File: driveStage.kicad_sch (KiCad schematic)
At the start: 20 parts

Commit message: minor improvements
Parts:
- added R?: 0, symbol Device:R
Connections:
- net at R?.2: now also R?.1; no longer R?.2
- new net: R?.2, R?.2
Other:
- note added: "40Hz Sallen-Key low-pass filter Works together with MAX5719 2k output resistance"
- note added: "For control loop response tuning ->"
- note added: "Modulation Depth"
- note removed: "40Hz Sallen-Key low-Pass filter Works together with MAX5719 2k output resistance"
- moved on the sheet: Q?, R?
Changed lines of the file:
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@@
     (stroke (width 0) (type default) (color 0 0 0 0))
   )
-  (wire (pts (xy 278.13 130.81) (xy 278.13 127))
+  (wire (pts (xy 289.56 130.81) (xy 289.56 127))
     (stroke (width 0) (type default) (color 0 0 0 0))
   )
@@
     (stroke (width 0) (type default) (color 0 0 0 0))
   )
-  (wire (pts (xy 271.78 156.21) (xy 274.32 156.21))
-    (stroke (width 0) (type default) (color 0 0 0 0))
-  )
   (wire (pts (xy 236.22 146.05) (xy 241.3 146.05))
     (stroke (width 0) (type default) (color 0 0 0 0))
@@
     (stroke (width 0) (type default) (color 0 0 0 0))
   )
-  (wire (pts (xy 260.35 135.89) (xy 270.51 135.89))
+  (wire (pts (xy 260.35 135.89) (xy 281.94 135.89))
     (stroke (width 0) (type default) (color 0 0 0 0))
   )
@@
     (stroke (width 0) (type default) (color 0 0 0 0))
   )
-  (wire (pts (xy 278.13 127) (xy 285.75 127))
+  (wire (pts (xy 289.56 127) (xy 297.18 127))
     (stroke (width 0) (type default) (color 0 0 0 0))
   )
@@
     (stroke (width 0) (type default) (color 0 0 0 0))
   )
-  (wire (pts (xy 260.35 161.29) (xy 274.32 161.29))
+  (wire (pts (xy 280.67 161.29) (xy 285.75 161.29))
     (stroke (width 0) (type default) (color 0 0 0 0))
   )
@@
     (stroke (width 0) (type default) (color 0 0 0 0))
   )
+  (wire (pts (xy 271.78 156.21) (xy 275.59 156.21))
+    (stroke (width 0) (type default) (color 0 0 0 0))
+  )
   (wire (pts (xy 163.83 163.83) (xy 163.83 166.37))
     (stroke (width 0) (type default) (color 0 0 0 0))
@@
     (stroke (width 0) (type default) (color 0 0 0 0))
   )
+  (wire (pts (xy 283.21 156.21) (xy 285.75 156.21))
+    (stroke (width 0) (type default) (color 0 0 0 0))
+  )
   (wire (pts (xy 171.45 110.49) (xy 185.42 110.49))
     (stroke (width 0) (type default) (color 0 0 0 0))
@@
     (stroke (width 0) (type default) (color 0 0 0 0))
   )
-  (wire (pts (xy 278.13 123.19) (xy 285.75 123.19))
+  (wire (pts (xy 289.56 123.19) (xy 297.18 123.19))
     (stroke (width 0) (type default) (color 0 0 0 0))
   )
@@
     (stroke (width 0) (type default) (color 0 0 0 0))
   )
-  (wire (pts (xy 278.13 118.11) (xy 278.13 123.19))
+  (wire (pts (xy 289.56 118.11) (xy 289.56 123.19))
     (stroke (width 0) (type default) (color 0 0 0 0))
   )
@@
     (stroke (width 0) (type default) (color 0 0 0 0))
   )
-  (wire (pts (xy 278.13 140.97) (xy 278.13 153.67))
+  (wire (pts (xy 289.56 140.97) (xy 289.56 153.67))
     (stroke (width 0) (type default) (color 0 0 0 0))
   )
@@
     (effects (font (size 1.27 1.27)) (justify left bottom))
   )
+  (text "For control loop\nresponse tuning\n   ->" (at 271.145 154.305 0)
+    (effects (font (size 1.27 1.27)) (justify left bottom))
+  )
   (text "25mA/V" (at 134.62 87.63 0)
     (effects (font (size 1.27 1.27)) (justify left bottom))
   )
-  (text "40Hz Sallen-Key low-Pass filter\n\nWorks together with MAX5719 2k output resistance"
+  (text "40Hz Sallen-Key low-pass filter\n\nWorks together with MAX5719 2k output resistance"
     (at 86.36 163.83 0)
     (effects (font (size 1.27 1.27)) (justify left bottom))
   )
-  (hierarchical_label "LD+" (shape output) (at 285.75 123.19 0)
+  (text "Modulation Depth" (at 127 80.01 0)
+    (effects (font (size 1.27 1.27)) (justify left bottom))
+  )
+  (hierarchical_label "LD+" (shape output) (at 297.18 123.19 0)
     (effects (font (size 1.27 1.27)) (justify left))
   )
-  (hierarchical_label "GND_SEN" (shape output) (at 260.35 161.29 180)
+  (hierarchical_label "GND_SEN" (shape output) (at 280.67 161.29 180)
     (effects (font (size 1.27 1.27)) (justify right))
   )
@@
     (effects (font (size 1.27 1.27)) (justify right))
   )
-  (hierarchical_label "LD-" (shape output) (at 285.75 127 0)
+  (hierarchical_label "LD-" (shape output) (at 297.18 127 0)
     (effects (font (size 1.27 1.27)) (justify left))
   )
@@
     )
     (property "Datasheet" "~" (id 3) (at 140.97 140.97 0)
+      (effects (font (size 1.27 1.27)) hide)
+    )
+    (pin "1")
+    (pin "2")
+  )
+  (symbol (lib_id "Device:R") (at 279.4 156.21 90) (unit 1)
+    (in_bom yes) (on_board yes)
+    (property "Reference" "R?" (id 0) (at 279.4 158.75 90))
+    (property "Value" "0" (id 1) (at 279.4 153.67 90))
+    (property "Footprint" "" (id 2) (at 279.4 157.988 90)
+      (effects (font (size 1.27 1.27)) hide)
+    )
+    (property "Datasheet" "~" (id 3) (at 279.4 156.21 0)
       (effects (font (size 1.27 1.27)) hide)
     )
@@
     (pin "1")
   )
-  (symbol (lib_id "Device:R_Shunt") (at 278.13 158.75 0) (mirror y) (unit 1)
-    (in_bom yes) (on_board yes) (fields_autoplaced)
-    (property "Reference" "R?" (id 0) (at 280.67 157.4799 0)
+  (symbol (lib_id "Device:R_Shunt") (at 289.56 158.75 0) (mirror y) (unit 1)
+    (in_bom yes) (on_board yes) (fields_autoplaced)
+    (property "Reference" "R?" (id 0) (at 292.1 157.4799 0)
       (effects (font (size 1.27 1.27)) (justify right))
     )
-    (property "Value" "R_Shunt" (id 1) (at 280.67 160.0199 0)
+    (property "Value" "R_Shunt" (id 1) (at 292.1 160.0199 0)
       (effects (font (size 1.27 1.27)) (justify right))
     )
-    (property "Footprint" "" (id 2) (at 279.908 158.75 90)
-      (effects (font (size 1.27 1.27)) hide)
-    )
-    (property "Datasheet" "~" (id 3) (at 278.13 158.75 0)
+    (property "Footprint" "" (id 2) (at 291.338 158.75 90)
+      (effects (font (size 1.27 1.27)) hide)
+    )
+    (property "Datasheet" "~" (id 3) (at 289.56 158.75 0)
       (effects (font (size 1.27 1.27)) hide)
     )
@@
     (pin "1")
   )
-  (symbol (lib_id "power:GND") (at 278.13 163.83 0) (unit 1)
-    (in_bom yes) (on_board yes) (fields_autoplaced)
-    (property "Reference" "#PWR?" (id 0) (at 278.13 170.18 0)
-      (effects (font (size 1.27 1.27)) hide)
-    )
-    (property "Value" "GND" (id 1) (at 278.13 168.91 0))
-    (property "Footprint" "" (id 2) (at 278.13 163.83 0)
-      (effects (font (size 1.27 1.27)) hide)
-    )
-    (property "Datasheet" "" (id 3) (at 278.13 163.83 0)
+  (symbol (lib_id "power:GND") (at 289.56 163.83 0) (unit 1)
+    (in_bom yes) (on_board yes) (fields_autoplaced)
+    (property "Reference" "#PWR?" (id 0) (at 289.56 170.18 0)
+      (effects (font (size 1.27 1.27)) hide)
+    )
+    (property "Value" "GND" (id 1) (at 289.56 168.91 0))
+    (property "Footprint" "" (id 2) (at 289.56 163.83 0)
+      (effects (font (size 1.27 1.27)) hide)
+    )
+    (property "Datasheet" "" (id 3) (at 289.56 163.83 0)
       (effects (font (size 1.27 1.27)) hide)
     )
@@
     (pin "2")
   )
-  (symbol (lib_id "power:+8V") (at 278.13 118.11 0) (unit 1)
-    (in_bom yes) (on_board yes) (fields_autoplaced)
-    (property "Reference" "#PWR?" (id 0) (at 278.13 121.92 0)
-      (effects (font (size 1.27 1.27)) hide)
-    )
-    (property "Value" "+8V" (id 1) (at 278.13 113.03 0))
-    (property "Footprint" "" (id 2) (at 278.13 118.11 0)
-      (effects (font (size 1.27 1.27)) hide)
-    )
-    (property "Datasheet" "" (id 3) (at 278.13 118.11 0)
+  (symbol (lib_id "power:+8V") (at 289.56 118.11 0) (unit 1)
+    (in_bom yes) (on_board yes) (fields_autoplaced)
+    (property "Reference" "#PWR?" (id 0) (at 289.56 121.92 0)
+      (effects (font (size 1.27 1.27)) hide)
+    )
+    (property "Value" "+8V" (id 1) (at 289.56 113.03 0))
+    (property "Footprint" "" (id 2) (at 289.56 118.11 0)
+      (effects (font (size 1.27 1.27)) hide)
+    )
+    (property "Datasheet" "" (id 3) (at 289.56 118.11 0)
       (effects (font (size 1.27 1.27)) hide)
     )
@@
     (pin "1")
   )
-  (symbol (lib_id "Transistor_FET:CSD17507Q5A") (at 275.59 135.89 0) (unit 1)
-    (in_bom yes) (on_board yes) (fields_autoplaced)
-    (property "Reference" "Q?" (id 0) (at 281.94 134.6199 0)
-      (effects (font (size 1.27 1.27)) (justify left))
-    )
-    (property "Value" "CSD17507Q5A" (id 1) (at 281.94 137.1599 0)
-      (effects (font (size 1.27 1.27)) (justify left))
-    )
-    (property "Footprint" "Package_TO_SOT_SMD:TDSON-8-1" (id 2) (at 280.67 137.795 0)
+  (symbol (lib_id "Transistor_FET:CSD17507Q5A") (at 287.02 135.89 0) (unit 1)
+    (in_bom yes) (on_board yes) (fields_autoplaced)
+    (property "Reference" "Q?" (id 0) (at 293.37 134.6199 0)
+      (effects (font (size 1.27 1.27)) (justify left))
+    )
+    (property "Value" "CSD17507Q5A" (id 1) (at 293.37 137.1599 0)
+      (effects (font (size 1.27 1.27)) (justify left))
+    )
+    (property "Footprint" "Package_TO_SOT_SMD:TDSON-8-1" (id 2) (at 292.1 137.795 0)
       (effects (font (size 1.27 1.27) italic) (justify left) hide)
     )
-    (property "Datasheet" "http://www.ti.com/lit/gpn/csd17507q5a" (id 3) (at 275.59 135.89 90)
+    (property "Datasheet" "http://www.ti.com/lit/gpn/csd17507q5a" (id 3) (at 287.02 135.89 90)
       (effects (font (size 1.27 1.27)) (justify left) hide)
     )

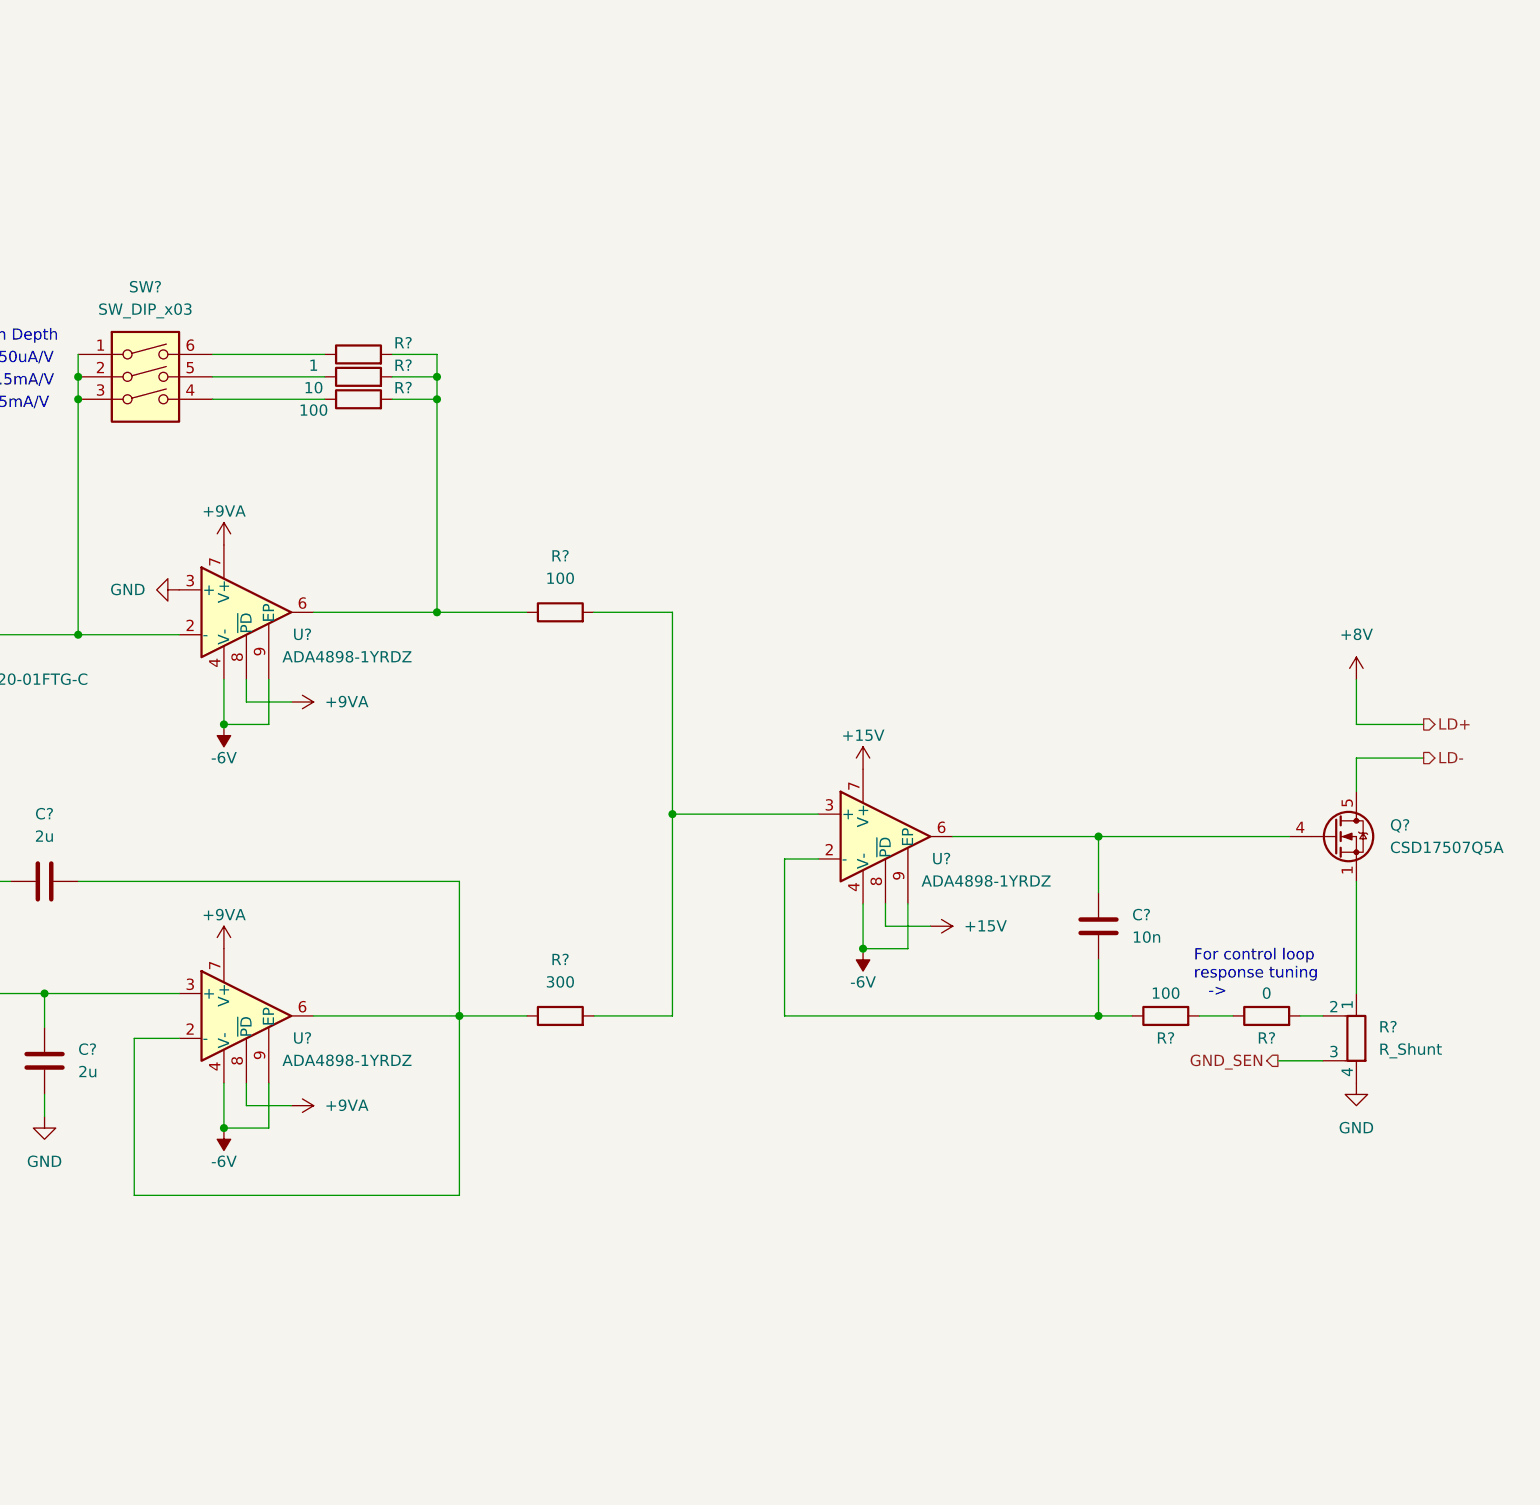
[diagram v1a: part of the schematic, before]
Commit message: add ref dac
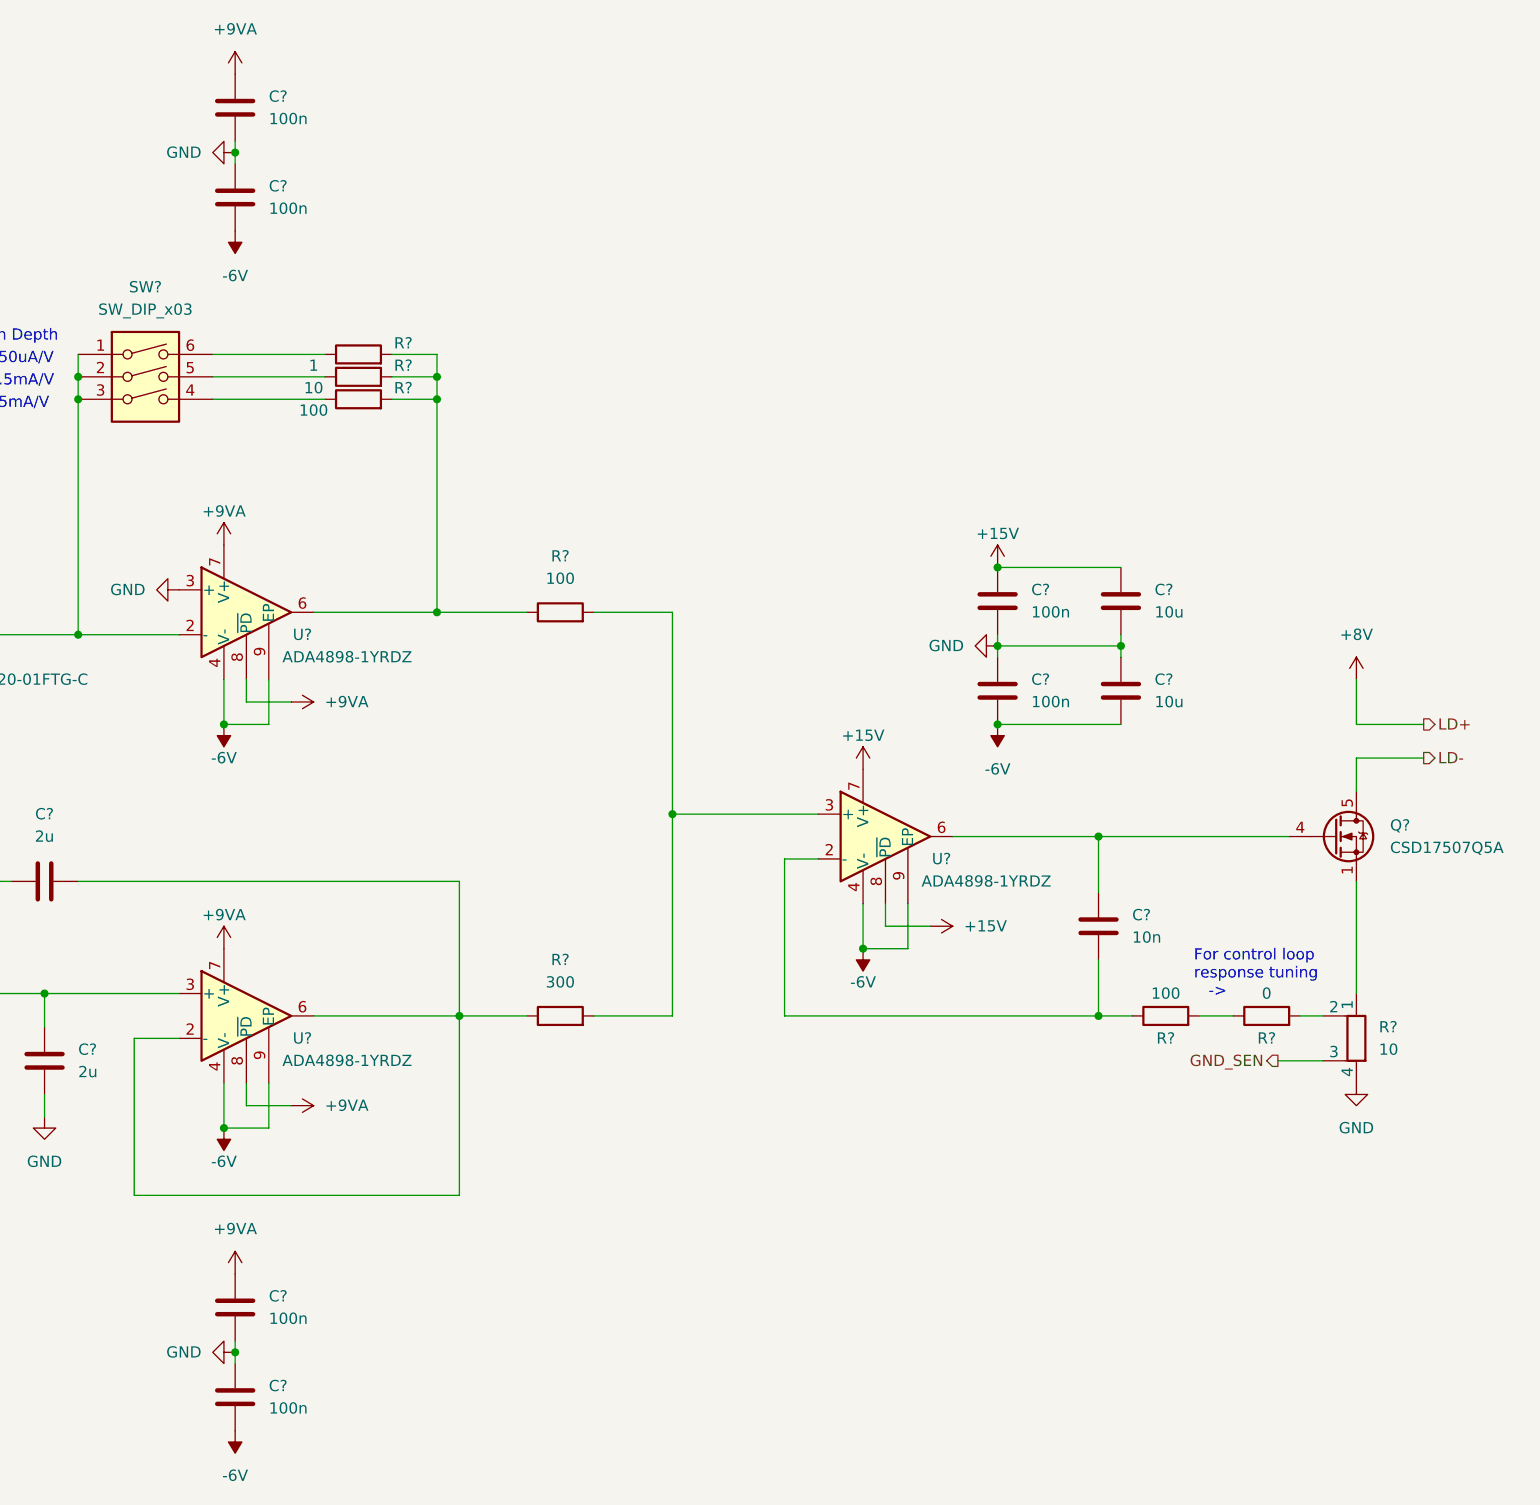
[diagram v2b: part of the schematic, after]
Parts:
- added C? (x2): 10u, symbol Device:C
- added C? (x6): 100n, symbol Device:C
- R?: value R_Shunt -> 10
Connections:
- net +15V: now also C?.1, C?.1
- net +9VA: now also C?.1, C?.1
- net -6V: now also C?.2, C?.2, C?.2, C?.2
- net GND: now also C?.1, C?.1, C?.1, C?.1, C?.2, C?.2, C?.2, C?.2

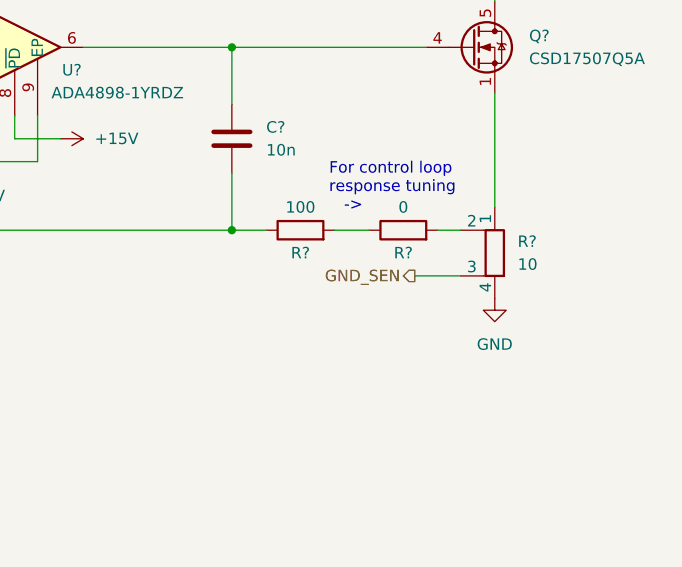
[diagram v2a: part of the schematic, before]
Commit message: finish drive stage, add sheets
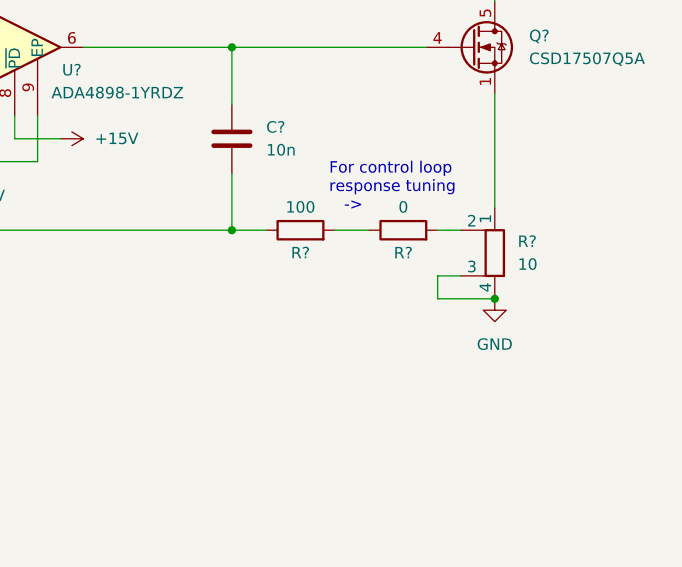
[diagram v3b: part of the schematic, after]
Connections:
- net GND_SEN is gone; now on net GND: R?.3
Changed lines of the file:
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@@
   (junction (at 260.35 156.21) (diameter 0) (color 0 0 0 0)
   )
+  (junction (at 289.56 163.83) (diameter 0) (color 0 0 0 0)
+  )
   (junction (at 260.35 135.89) (diameter 0) (color 0 0 0 0)
   )
@@
     (stroke (width 0) (type default) (color 0 0 0 0))
   )
+  (wire (pts (xy 283.21 161.29) (xy 283.21 163.83))
+    (stroke (width 0) (type default) (color 0 0 0 0))
+  )
   (wire (pts (xy 185.42 110.49) (xy 195.58 110.49))
     (stroke (width 0) (type default) (color 0 0 0 0))
@@
     (stroke (width 0) (type default) (color 0 0 0 0))
   )
-  (wire (pts (xy 280.67 161.29) (xy 285.75 161.29))
+  (wire (pts (xy 283.21 161.29) (xy 285.75 161.29))
     (stroke (width 0) (type default) (color 0 0 0 0))
   )
@@
   )
   (wire (pts (xy 156.21 158.75) (xy 151.13 158.75))
+    (stroke (width 0) (type default) (color 0 0 0 0))
+  )
+  (wire (pts (xy 283.21 163.83) (xy 289.56 163.83))
     (stroke (width 0) (type default) (color 0 0 0 0))
   )
@@
     (effects (font (size 1.27 1.27)) (justify left))
   )
-  (hierarchical_label "GND_SEN" (shape output) (at 280.67 161.29 180)
-    (effects (font (size 1.27 1.27)) (justify right))
-  )
   (hierarchical_label "LD_DAC" (shape input) (at 93.98 153.67 180)
